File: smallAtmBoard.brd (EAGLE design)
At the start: 66.1 x 51.7 mm, 29 parts, among them IC1 ATMEGA-328P, IC2 7805-V, Y1 16MHz

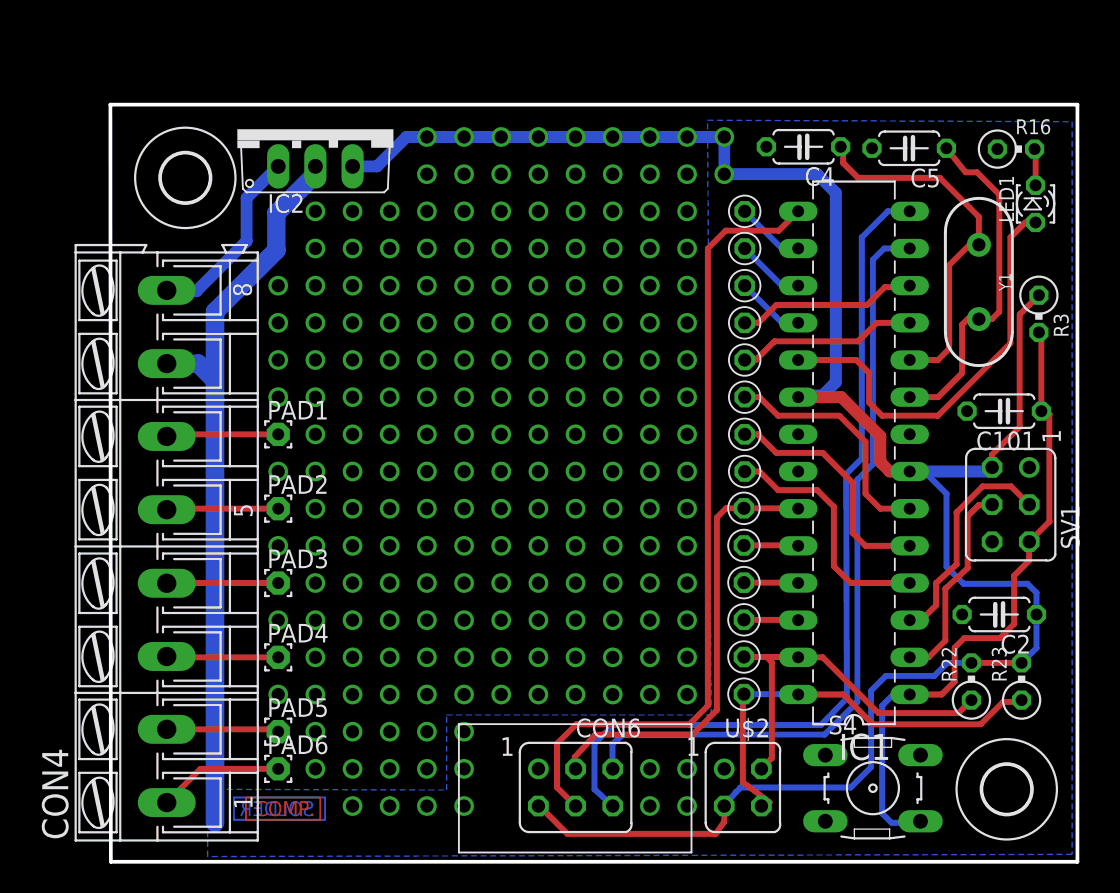
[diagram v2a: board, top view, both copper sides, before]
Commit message: move 7805 and change connector
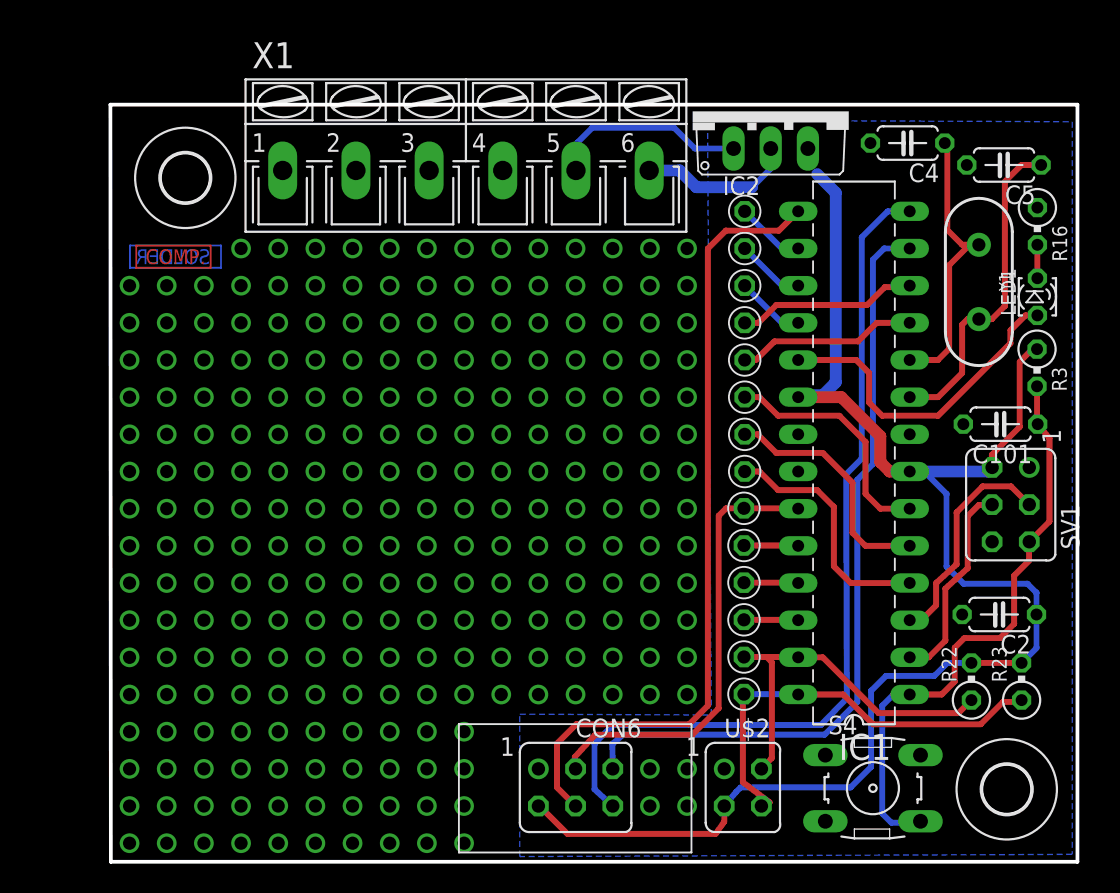
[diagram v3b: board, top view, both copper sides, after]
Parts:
- removed CON4: (no value), bauteile_jbt:AK300/8
- removed PAD1, PAD2, PAD3, PAD4, PAD5, PAD6: D1, bauteile_jbt:PAD1,6/0,8
- added X1: (no value), bauteile_jbt:AK300/6
- IC2: value 7805-V -> 7805
- moved U$7 38.5 mm to (4.14, 41.4)
- moved U$6 38.4 mm to (4.60, 41.4)
- moved IC2 31.1 mm to (45.1, 51.3)
- moved C4 7.12 mm to (54.4, 49.1)
- moved C5 6.58 mm to (61.0, 47.6)
- moved LED1 6.35 mm to (63.3, 38.6)
- moved R16 5.47 mm to (63.3, 43.4), turned to 270 degrees
- moved R3 3.69 mm to (63.3, 33.8)
- moved C101 0.92 mm to (60.8, 29.9)
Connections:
- removed net N$21: CON4.6, PAD1.1
- removed net N$22: CON4.5, PAD2.1
- removed net N$23: CON4.4, PAD3.1
- removed net N$24: CON4.3, PAD4.1
- removed net N$25: CON4.2, PAD5.1
- removed net N$26: CON4.1, PAD6.1
- net +12V: now also X1.5; no longer CON4.8
- net GND: now also X1.6; no longer CON4.7
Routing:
- net GND: track 51.7 -> 10.7 mm, vias 3 -> 0
- net VCC: track 144.3 -> 105.6 mm, vias 10 -> 0
- net N$26: track 8.57 -> 0.00 mm, vias 0 -> 1
- net N$25: track 7.69 -> 0.00 mm, vias 0 -> 1
- net N$21: track 7.68 -> 0.00 mm, vias 0 -> 1
- net N$22: track 7.65 -> 0.00 mm, vias 0 -> 1
- net N$24: track 7.64 -> 0.00 mm, vias 0 -> 1
- net N$23: track 7.63 -> 0.00 mm, vias 0 -> 1
- net AT-PD13: track 28.7 -> 22.5 mm
- net XTAL2: track 25.2 -> 19.9 mm
- net RESET: track 44.3 -> 40.5 mm
- net XTAL1: track 23.5 -> 22.5 mm
- net +12V: track 12.9 -> 13.6 mm
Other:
- board text removed: "GND"
